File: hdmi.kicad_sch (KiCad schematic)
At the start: 10 parts, among them J6 HDMI_A, U4 AP22615AWU

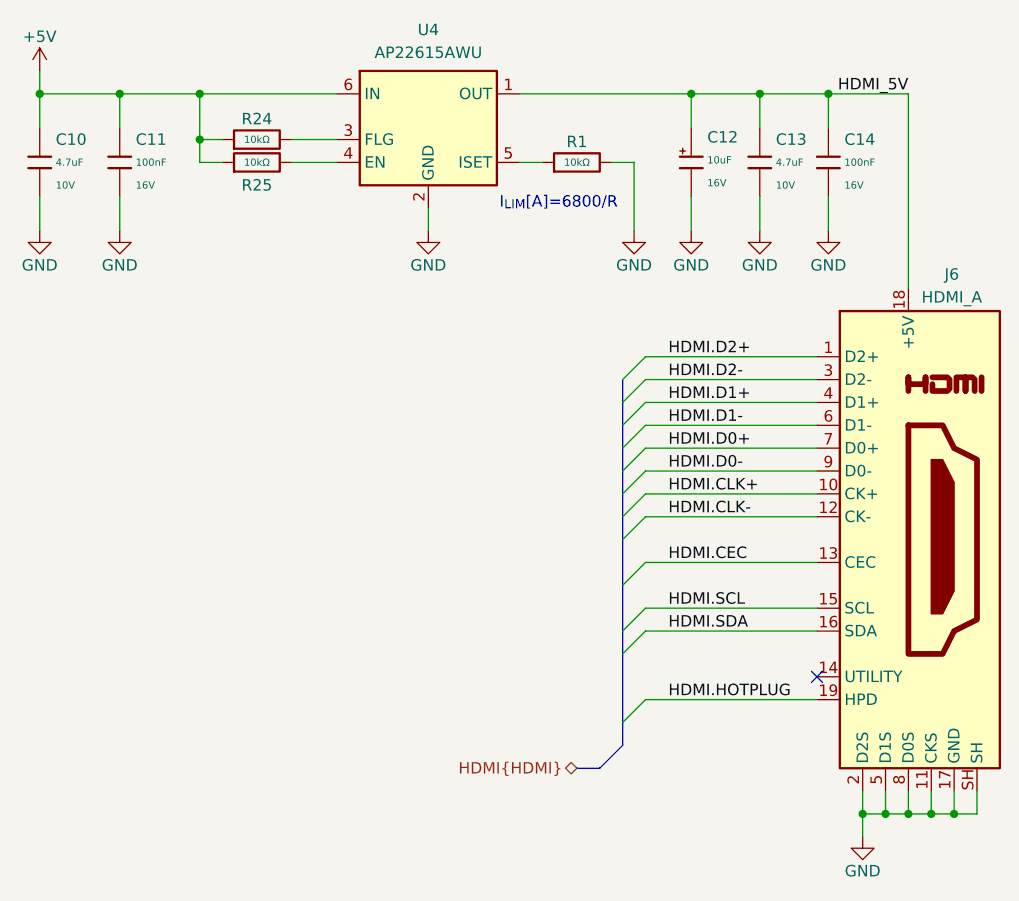
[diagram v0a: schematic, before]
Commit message: [#1] WIP: Change components to ones from the global library, refactor schematic
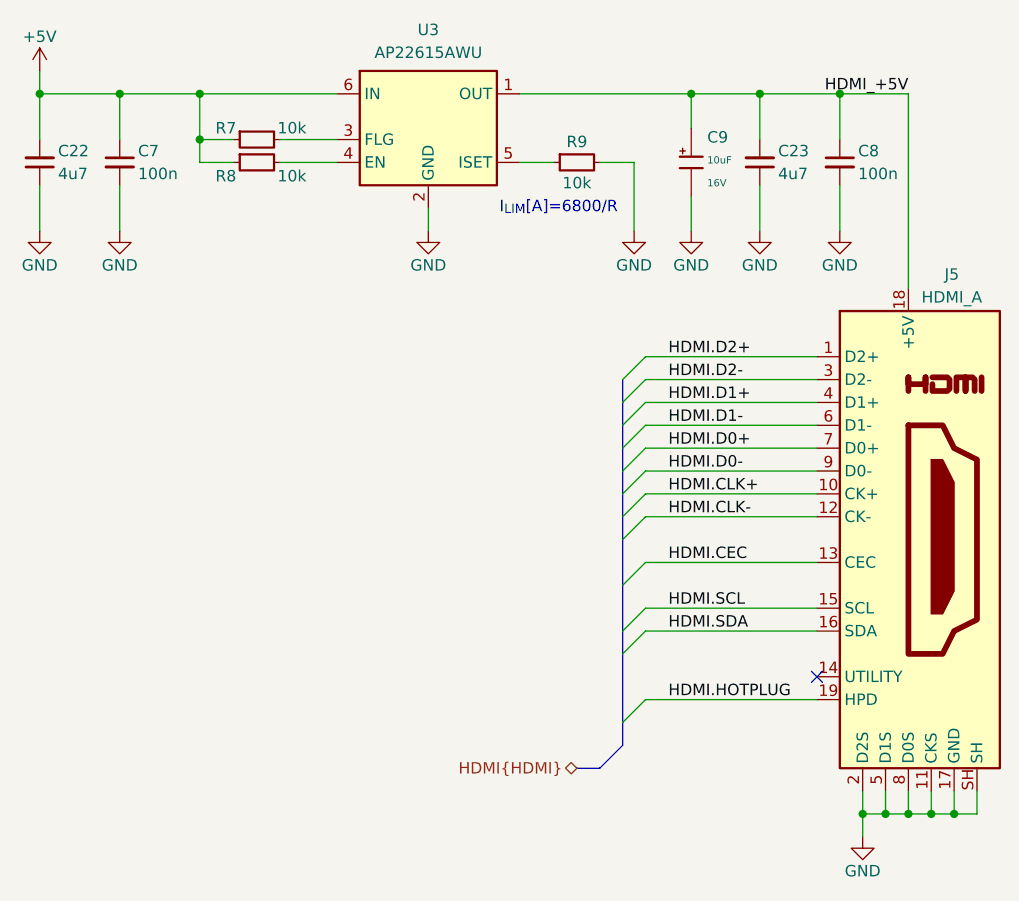
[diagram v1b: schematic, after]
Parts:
- removed C10, C13: 4.7uF, PCM_JLCPCB:C_0402, symbol PCM_JLCPCB-Capacitors:0402,4.7uF
- removed C11, C14: 100nF, PCM_JLCPCB:C_0402, symbol PCM_JLCPCB-Capacitors:0402,100nF
- removed R1, R24, R25: 10kΩ, PCM_JLCPCB:R_0402, symbol PCM_JLCPCB-Resistors:0402,10kΩ
- added C22, C23: C-4u7-0402, DW-footprints:C_0402_1005Metric, symbol DW-capacitors:C-4u7-0402
- added C7, C8: C-100n-0402, DW-footprints:C_0402_1005Metric, symbol DW-capacitors:C-100n-0402
- added R7, R8, R9: R-10k-0402, DW-footprints:R_0402_1005Metric, symbol DW-resistors:R-10k-0402
- renumbered C12 to C9, J6 to J5, U4 to U3
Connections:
- net +5V: now also C22.2, C7.1, R7.1, R8.1
- net GND: now also C22.1, C23.1, C7.2, C8.2, R9.2
- net at U3.5 (ISET): now also R9.1
- net at U3.3 (FLG): now also R7.2
- net at U3.4 (EN): now also R8.2
- net HDMI_5V renamed HDMI_+5V
- net HDMI_+5V: now also C23.2, C8.1
